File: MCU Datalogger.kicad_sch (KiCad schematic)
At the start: 25 parts, among them U1 24LC1025, U2 24LC1025, U3 DS1337S_, U4 ATMEGA328P-AU, Y1 Crystal, Y2 Crystal

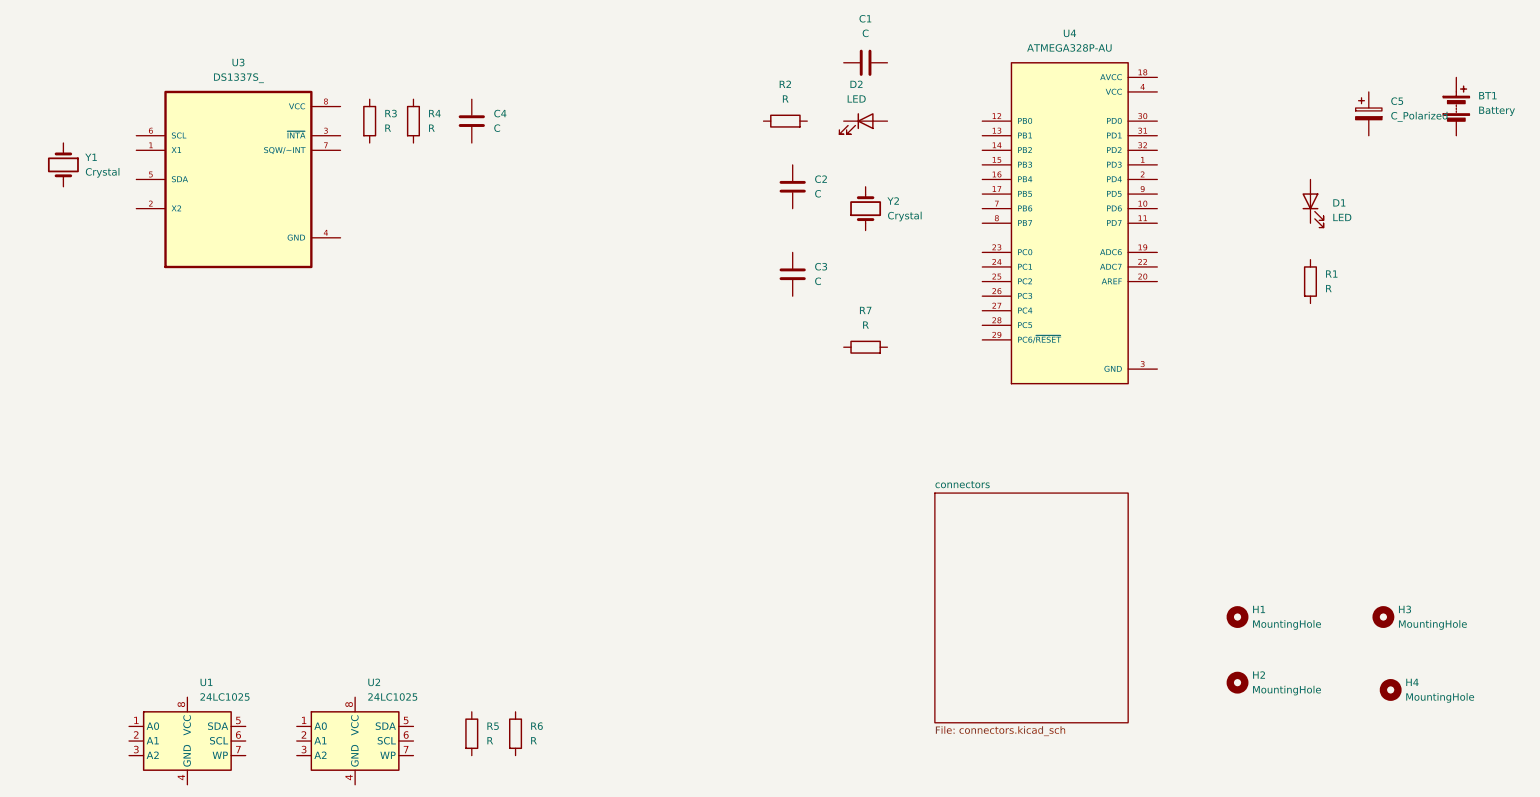
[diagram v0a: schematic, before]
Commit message: Added component values.
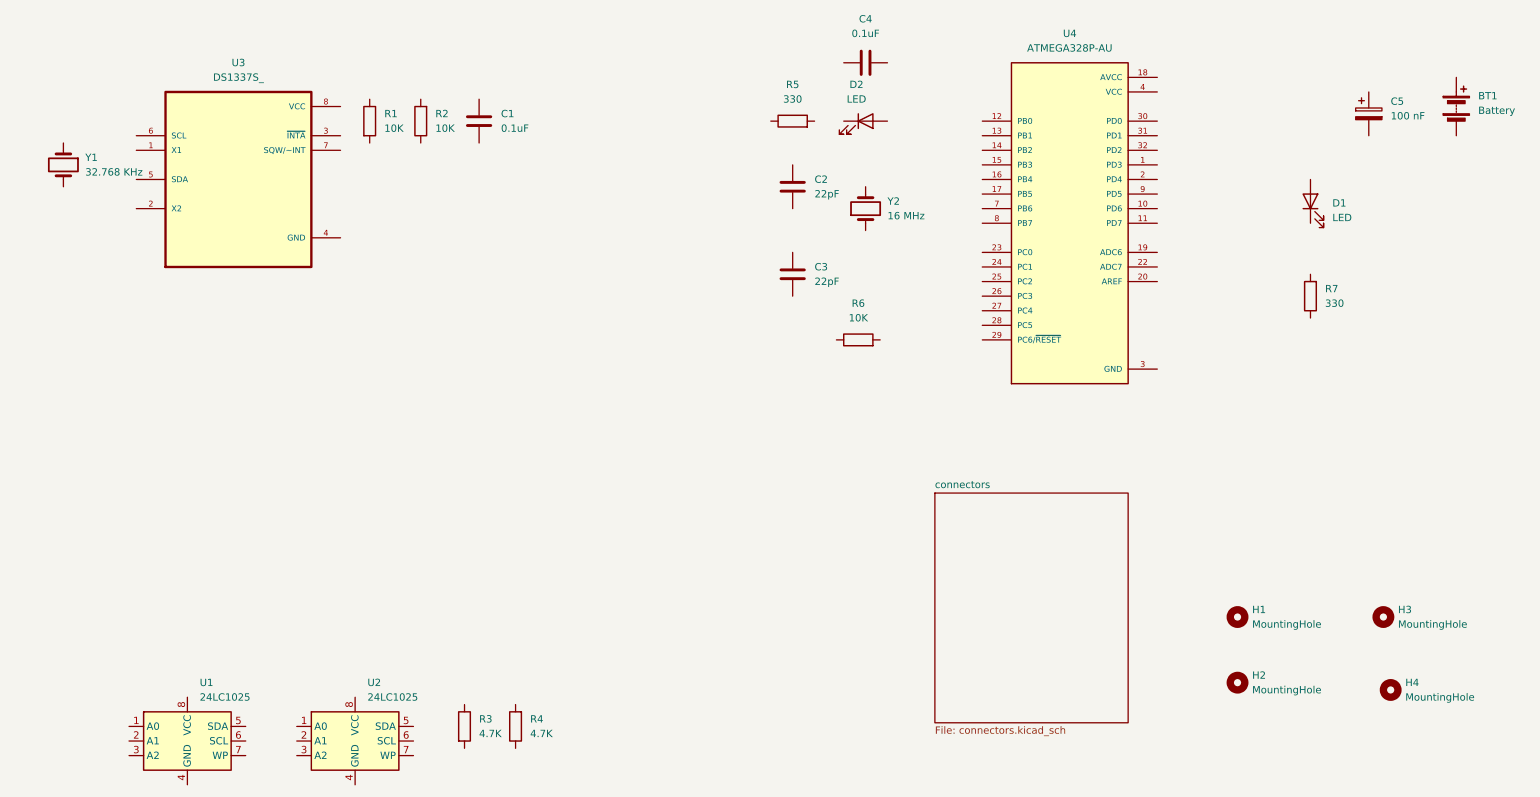
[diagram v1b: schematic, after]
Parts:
- C1, C4: value C -> 0.1uF
- C2, C3: value C -> 22pF
- C5: value C_Polarized -> 100 nF
- R1, R2, R6: value R -> 10K
- R3, R4: value R -> 4.7K
- R5, R7: value R -> 330
- Y1: value Crystal -> 32.768 KHz
- Y2: value Crystal -> 16 MHz
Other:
- moved on the sheet: C1, C4, R1, R2, R3, R4, R5, R6, R7

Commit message: Completed symbol-footprint associations.
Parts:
- BT1: footprint (none) -> Connector_PinHeader_2.54mm:PinHeader_1x02_P2.54mm_Vertical
- C1, C2, C3, C4, C5: footprint (none) -> Capacitor_SMD:C_0805_2012Metric
- D1, D2: footprint (none) -> LED_SMD:LED_0805_2012Metric
- H1, H2, H3, H4: footprint (none) -> MountingHole:MountingHole_2.1mm
- R1, R2, R3, R4, R5, R6, R7: footprint (none) -> Resistor_SMD:R_0805_2012Metric
- U1, U2: footprint (none) -> Package_SO:SOIC-8_5.3x5.3mm_P1.27mm
- U3: footprint DS1337S_:SOIC127P600X175-8N -> Footprints:SOIC127P600X175-8N
- U4: footprint ATMEGA328P-AU:QFP80P900X900X120-32N -> Footprints:QFP80P900X900X120-32N
- Y1, Y2: footprint (none) -> Crystal:Crystal_SMD_5032-2Pin_5.0x3.2mm_HandSoldering
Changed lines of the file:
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@@
 			)
 		)
-		(property "Footprint" ""
+		(property "Footprint" "Resistor_SMD:R_0805_2012Metric"
 			(at 94.742 158.75 90)
 			(effects
@@
 			)
 		)
-		(property "Footprint" ""
+		(property "Footprint" "Package_SO:SOIC-8_5.3x5.3mm_P1.27mm"
 			(at 48.26 161.29 0)
 			(effects
@@
 			)
 		)
-		(property "Footprint" ""
+		(property "Footprint" "Capacitor_SMD:C_0805_2012Metric"
 			(at 170.18 42.2148 0)
 			(effects
@@
 			)
 		)
-		(property "Footprint" ""
+		(property "Footprint" "Resistor_SMD:R_0805_2012Metric"
 			(at 90.678 53.34 90)
 			(effects
@@
 			)
 		)
-		(property "Footprint" ""
+		(property "Footprint" "Capacitor_SMD:C_0805_2012Metric"
 			(at 98.0948 49.53 0)
 			(effects
@@
 			)
 		)
-		(property "Footprint" ""
+		(property "Footprint" "Resistor_SMD:R_0805_2012Metric"
 			(at 165.1 93.218 90)
 			(effects
@@
 			)
 		)
-		(property "Footprint" ""
+		(property "Footprint" "Capacitor_SMD:C_0805_2012Metric"
 			(at 254.9652 55.88 0)
 			(effects
@@
 			)
 		)
-		(property "Footprint" ""
+		(property "Footprint" "Resistor_SMD:R_0805_2012Metric"
 			(at 78.232 53.34 90)
 			(effects
@@
 			)
 		)
-		(property "Footprint" ""
+		(property "Footprint" "Crystal:Crystal_SMD_5032-2Pin_5.0x3.2mm_HandSoldering"
 			(at 166.37 68.58 0)
 			(effects
@@
 			)
 		)
-		(property "Footprint" "DS1337S_:SOIC127P600X175-8N"
+		(property "Footprint" "Footprints:SOIC127P600X175-8N"
 			(at 57.15 63.5 0)
 			(effects
@@
 			)
 		)
-		(property "Footprint" ""
+		(property "Footprint" "Crystal:Crystal_SMD_5032-2Pin_5.0x3.2mm_HandSoldering"
 			(at 26.67 60.96 0)
 			(effects
@@
 			)
 		)
-		(property "Footprint" ""
+		(property "Footprint" "Resistor_SMD:R_0805_2012Metric"
 			(at 107.188 158.75 90)
 			(effects
@@
 			)
 		)
-		(property "Footprint" ""
+		(property "Footprint" "Capacitor_SMD:C_0805_2012Metric"
 			(at 154.6352 68.58 0)
 			(effects
@@
 			)
 		)
-		(property "Footprint" ""
+		(property "Footprint" "Connector_PinHeader_2.54mm:PinHeader_1x02_P2.54mm_Vertical"
 			(at 269.24 49.276 90)
 			(effects
@@
 			)
 		)
-		(property "Footprint" ""
+		(property "Footprint" "LED_SMD:LED_0805_2012Metric"
 			(at 166.37 53.34 0)
 			(effects
@@
 			)
 		)
-		(property "Footprint" "ATMEGA328P-AU:QFP80P900X900X120-32N"
+		(property "Footprint" "Footprints:QFP80P900X900X120-32N"
 			(at 201.93 71.12 0)
 			(effects
@@
 			)
 		)
-		(property "Footprint" ""
+		(property "Footprint" "MountingHole:MountingHole_2.1mm"
 			(at 231.14 139.7 0)
 			(effects
@@
 			)
 		)
-		(property "Footprint" ""
+		(property "Footprint" "Resistor_SMD:R_0805_2012Metric"
 			(at 153.67 55.118 90)
 			(effects
@@
 			)
 		)
-		(property "Footprint" ""
+		(property "Footprint" "MountingHole:MountingHole_2.1mm"
 			(at 257.81 152.4 0)
 			(effects
@@
 			)
 		)
-		(property "Footprint" ""
+		(property "Footprint" "Package_SO:SOIC-8_5.3x5.3mm_P1.27mm"
 			(at 77.47 161.29 0)
 			(effects
@@
 			)
 		)
-		(property "Footprint" ""
+		(property "Footprint" "Capacitor_SMD:C_0805_2012Metric"
 			(at 154.6352 83.82 0)
 			(effects
@@
 			)
 		)
-		(property "Footprint" ""
+		(property "Footprint" "MountingHole:MountingHole_2.1mm"
 			(at 256.54 139.7 0)
 			(effects
@@
 			)
 		)
-		(property "Footprint" ""
+		(property "Footprint" "MountingHole:MountingHole_2.1mm"
 			(at 231.14 151.13 0)
 			(effects
@@
 			)
 		)
-		(property "Footprint" ""
+		(property "Footprint" "Resistor_SMD:R_0805_2012Metric"
 			(at 245.618 83.82 90)
 			(effects
@@
 			)
 		)
-		(property "Footprint" ""
+		(property "Footprint" "LED_SMD:LED_0805_2012Metric"
 			(at 243.84 67.31 0)
 			(effects

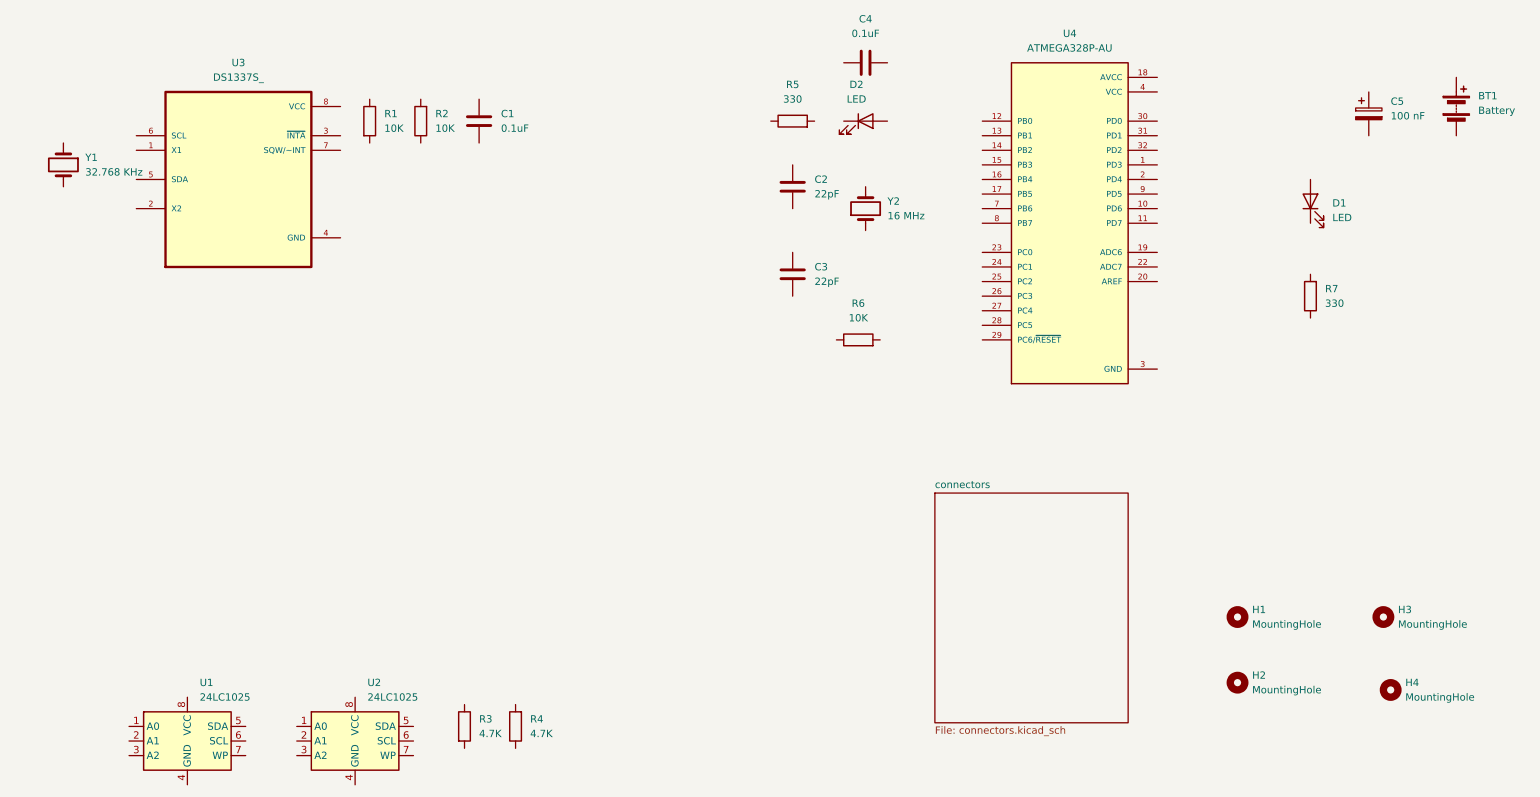
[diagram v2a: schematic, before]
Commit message: Completed wiring on main sheet.
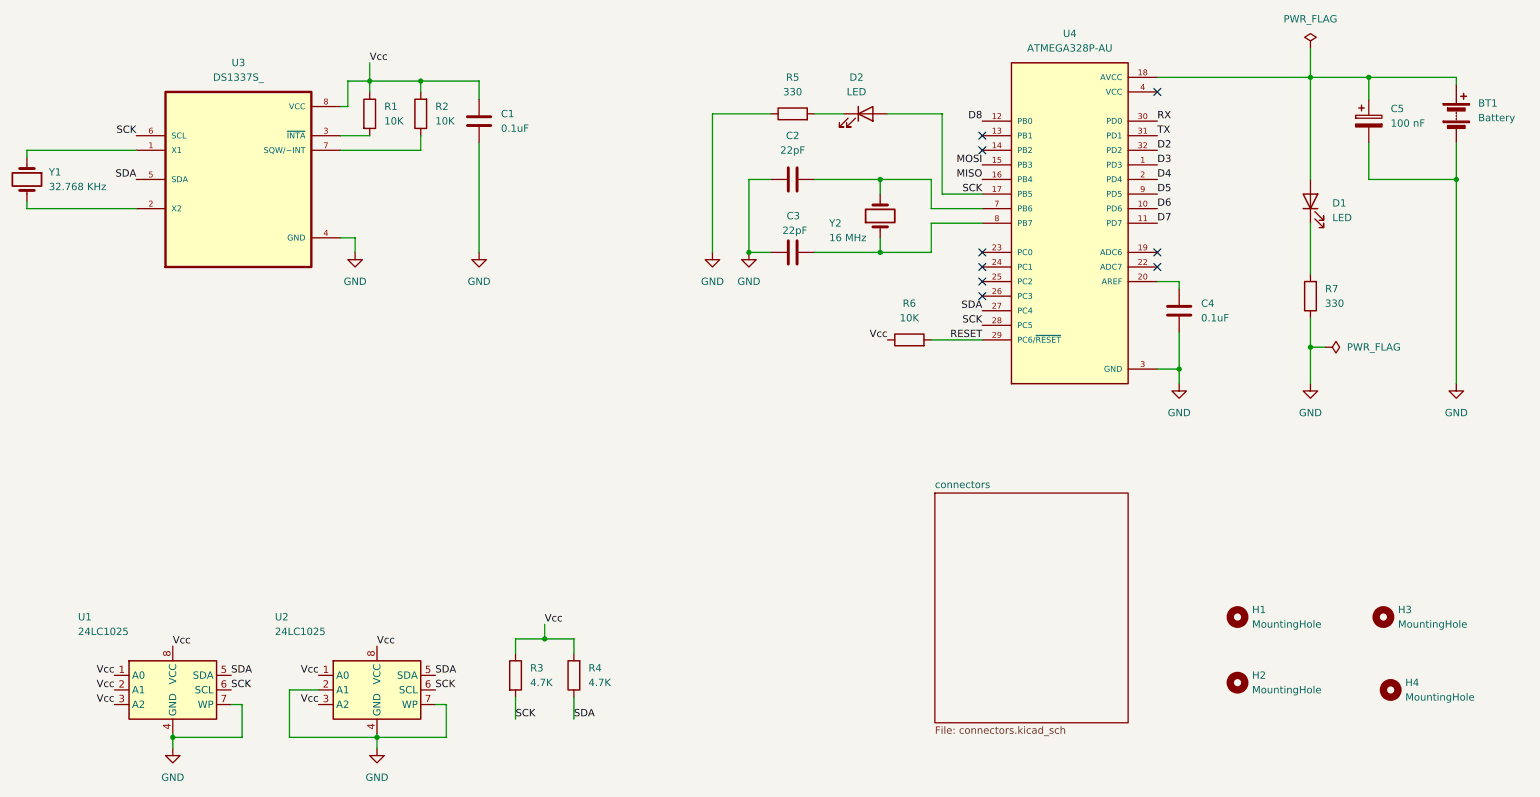
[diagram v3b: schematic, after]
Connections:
- net GND: now also BT1.2 (-), C1.1, C2.1, C3.1, C4.1, C5.2, R5.1, R7.1, U1.4 (GND), U1.7 (WP), U2.2 (A1), U2.4 (GND), U2.7 (WP), U3.4 (GND)
- net Vcc: now reaches R3.1
- net Vcc: now also C1.2, R1.1, R2.2, R4.2, R6.1, U1.1 (A0), U1.2 (A1), U1.3 (A2), U1.8 (VCC), U2.1 (A0), U2.3 (A2), U2.8 (VCC), U3.8 (VCC)
- net SCK: now reaches R3.2
- net SCK: now also D2.2 (A), U1.6 (SCL), U2.6 (SCL), U3.6 (SCL), U4.17 (PB5), U4.28 (PC5)
- net SDA: now reaches U1.5 (SDA)
- net SDA: now also R4.1, U2.5 (SDA), U3.5 (SDA), U4.27 (PC4)
- net at C4.2: now also U4.20 (AREF)
- net at R2.1: now also U3.7 (SQW/~INT)
- net RESET: now reaches R6.2
- net RESET: now also U4.29 (PC6/~{RESET})
- net at C5.1: now also BT1.1 (+), D1.2 (A), U4.18 (AVCC)
- net at R1.2: now also U3.3 (~{INTA})
- net at Y2.1: now also C3.2, U4.8 (PB7)
- net at Y2.2: now also C2.2, U4.7 (PB6)
- net at U3.1 (X1): now also Y1.1
- net at U3.2 (X2): now also Y1.2
- net at D2.1 (K): now also R5.2
- net D3: now reaches U4.1 (PD3)
- net D6: now reaches U4.10 (PD6)
- net D7: now reaches U4.11 (PD7)
- net D8: now reaches U4.12 (PB0)
- net MOSI: now reaches U4.15 (PB3)
- net MISO: now reaches U4.16 (PB4)
- net D4: now reaches U4.2 (PD4)
- net RX: now reaches U4.30 (PD0)
- net TX: now reaches U4.31 (PD1)
- net D2: now reaches U4.32 (PD2)
- net D5: now reaches U4.9 (PD5)
- net at R7.2: now also D1.1 (K)
- no-connect marks 0 -> 9
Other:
- moved on the sheet: BT1, C2, C3, C4, C5, D2, R1, R2, R3, R4, R5, R6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

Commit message: Completed wiring in the second sheet.
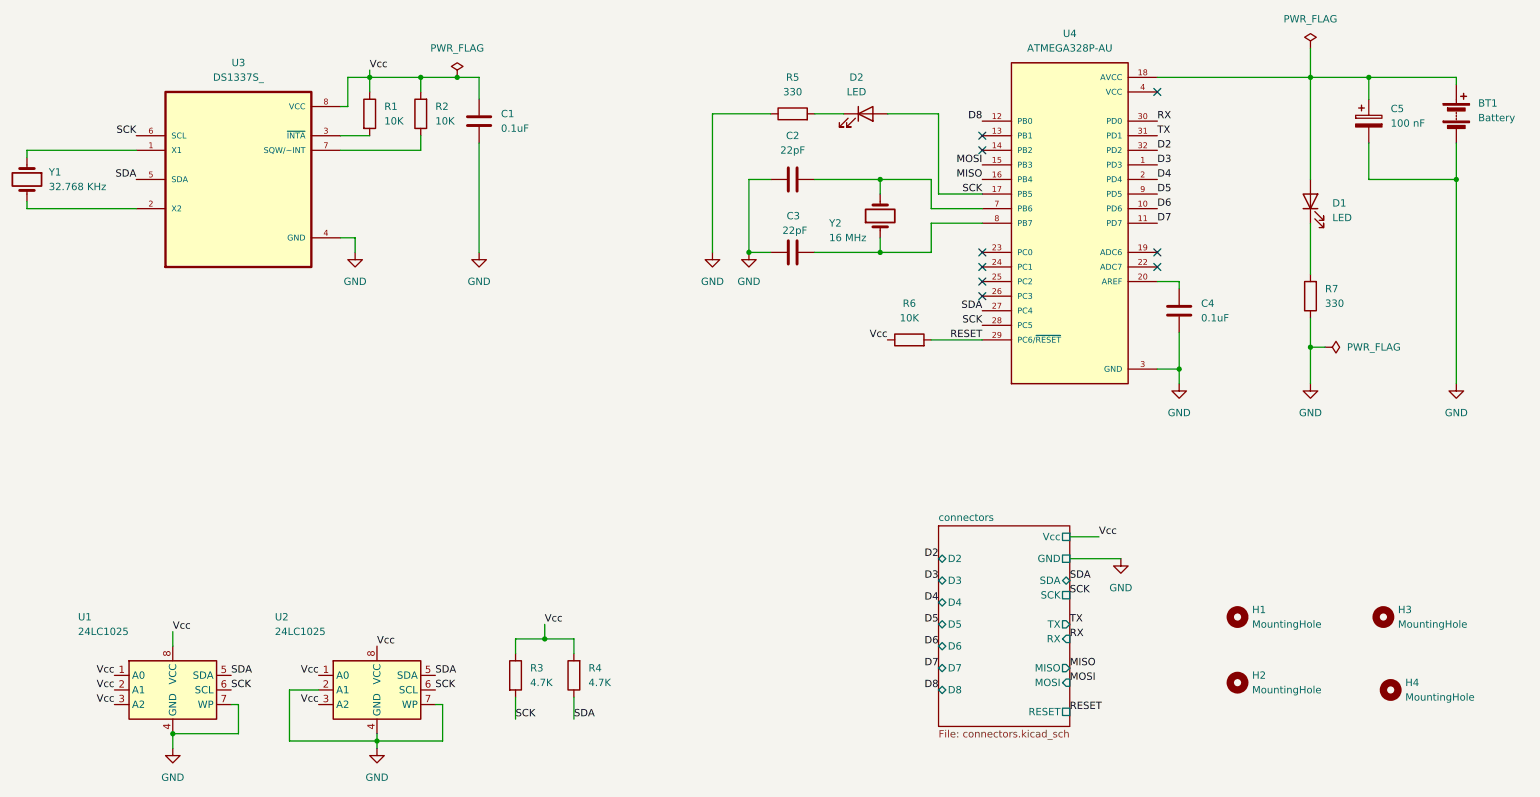
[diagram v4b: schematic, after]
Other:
- sheet connectors ports: added D2, D3, D4, D5, D6, D7, D8, GND, MISO, MOSI, RESET, RX, SCK, SDA, TX, Vcc; removed none
